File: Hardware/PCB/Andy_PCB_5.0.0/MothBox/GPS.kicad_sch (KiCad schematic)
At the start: 46 parts, among them J4 GPS Header, SW2 Days, SW3 Power, SW4 Sequence+Toggle, SW5 Hours, SW6 Hours, U12 CD74HC4067M96E4, U13 CD74HC4067M96E4

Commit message: made better camera
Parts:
- renumbered C18 to C16, C13 to C17, R28 to R16, R16 to R17, R29 to R18, R17 to R19, R30 to R20, R83 to R21, R18 to R22, R84 to R23, R31 to R24, R85 to R25, R86 to R26, R32 to R27, R19 to R28, R33 to R29, R34 to R30, R20 to R31, R35 to R32, R21 to R33, R36 to R34, R22 to R35, R37 to R36, R23 to R37, R47 to R39, R24 to R40, R39 to R41, R48 to R42, R49 to R43, R50 to R44, R40 to R45, R25 to R46, R41 to R47, R26 to R48, R42 to R49, R27 to R50, U12 to U8, U13 to U9

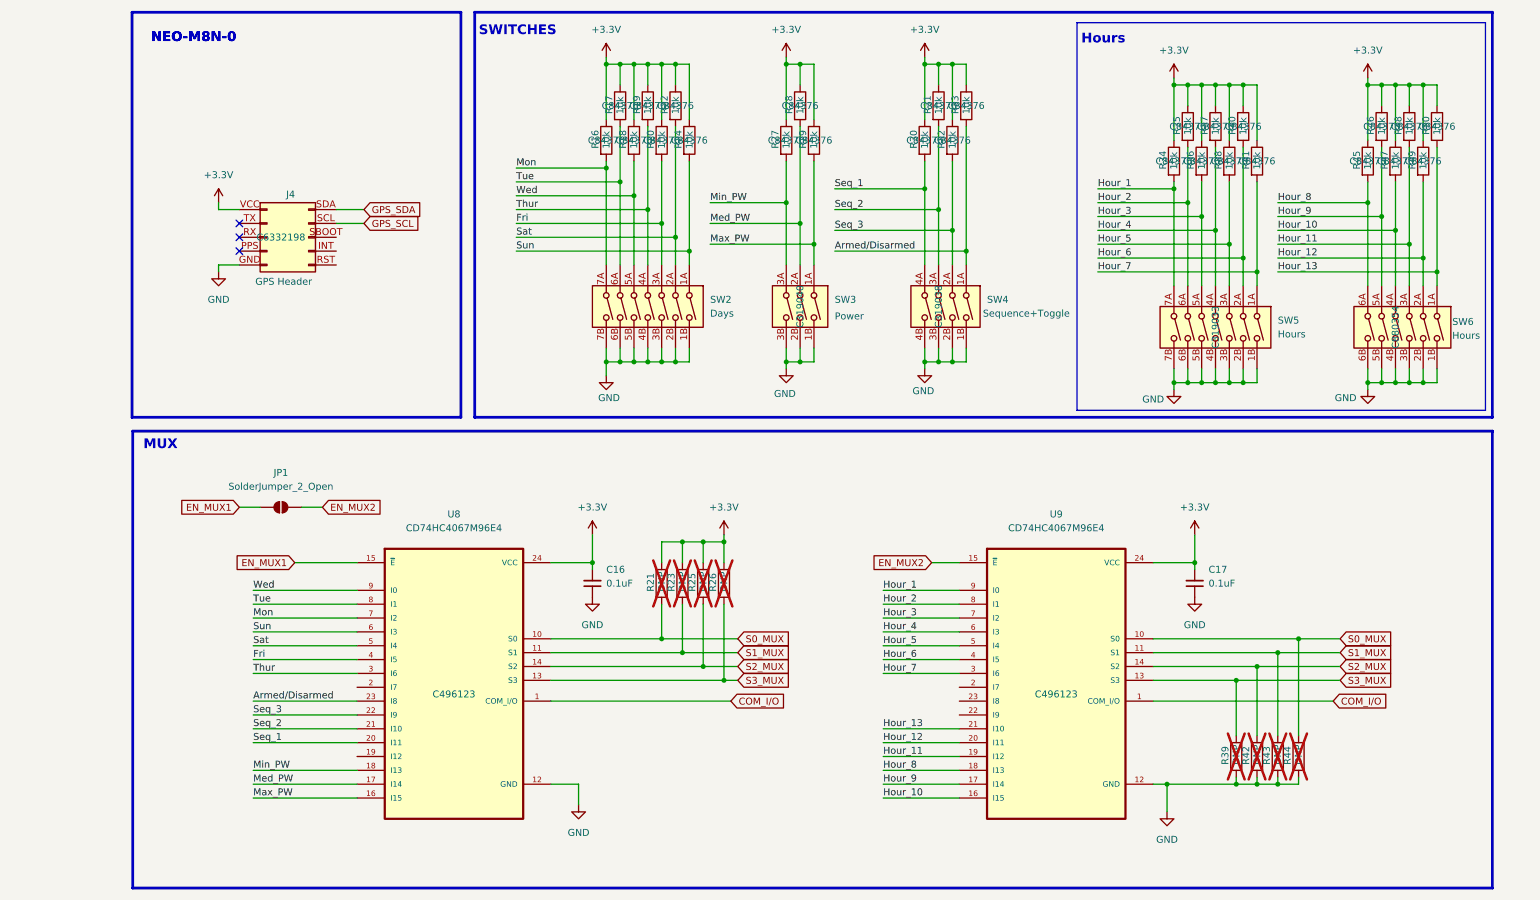
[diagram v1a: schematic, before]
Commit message: added female inverted header
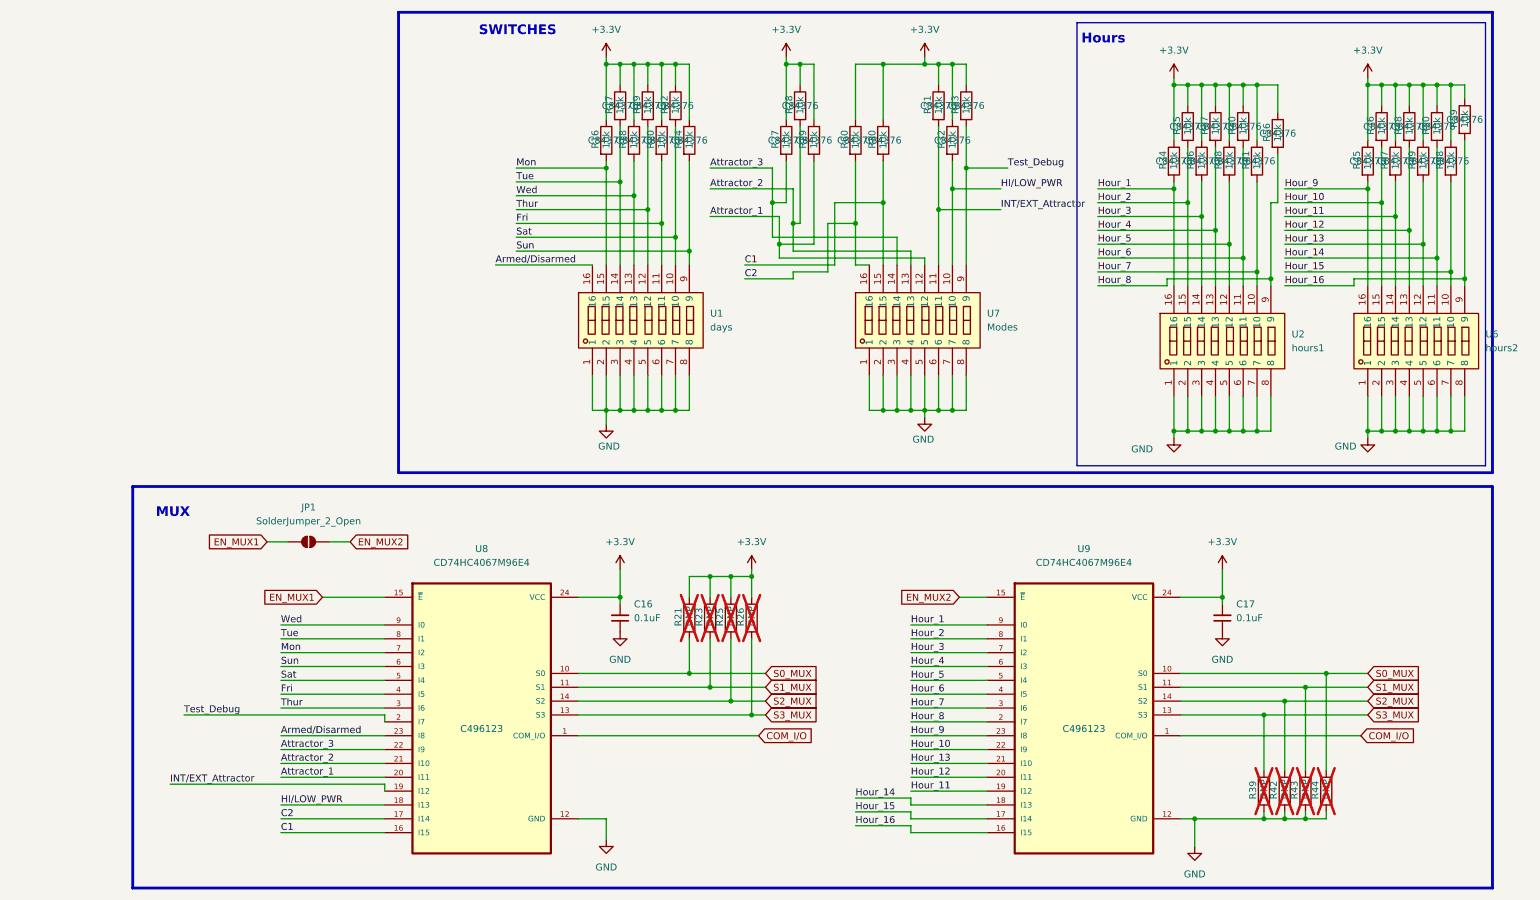
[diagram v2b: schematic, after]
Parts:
- removed J4: GPS Header, GPS_MAX10:Untitled, symbol Connector:DIN41612_02x05_AC_EvenPins
- removed SW2: Days, DS04-254-2-07BK-SMT:SW_DS04-254-2-07BK-SMT, symbol Switch:SW_DIP_x07
- removed SW3: Power, DS04-254-2-03BK-SMT1:SW_DS04-254-2-03BK-SMT, symbol Switch:SW_DIP_x03
- removed SW4: Sequence+Toggle, DS04-254-2-04BK-SMT:SW_DS04-254-2-04BK-SMT, symbol Switch:SW_DIP_x04
- removed SW5: Hours, DS04-254-2-07BK-SMT:SW_DS04-254-2-07BK-SMT, symbol Switch:SW_DIP_x07
- removed SW6: Hours, DS04-254-2-06BK-SMT:SW_DS04-254-2-06BK-SMT, symbol Switch:SW_DIP_x06
- added R56, R58, R59, R60: 10k, Resistor_SMD:R_0805_2012Metric, symbol Device:R
- added U1: days, easyeda2kicad:SW-TH_16P-L21.7-W9.7-P2.54-BL, symbol easyeda2kicad:SMQS-08R-TP
- added U2: hours1, easyeda2kicad:SW-TH_16P-L21.7-W9.7-P2.54-BL, symbol easyeda2kicad:SMQS-08R-TP
- added U6: hours2, easyeda2kicad:SW-TH_16P-L21.7-W9.7-P2.54-BL, symbol easyeda2kicad:SMQS-08R-TP
- added U7: Modes, easyeda2kicad:SW-TH_16P-L21.7-W9.7-P2.54-BL, symbol easyeda2kicad:SMQS-08R-TP
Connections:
- net +3.3V: now also R56.1, R58.1, R59.1, R60.1
- net Armed/Disarmed: now also U1.16; no longer R33.2
- net Fri: now also U1.11
- net GND: now also U1.1, U1.2, U1.3, U1.4, U1.5, U1.6, U1.7, U1.8, U2.1, U2.2, U2.3, U2.4, U2.5, U2.6, U2.7, U2.8, U6.1, U6.2, U6.3, U6.4, U6.5, U6.6, U6.7, U6.8, U7.1, U7.2, U7.3, U7.4, U7.5, U7.6, U7.7, U7.8
- net Hour_1: now also U2.16
- net Hour_10: now also R46.2, U9.22 (I9), U6.15; no longer R47.2, U9.16 (I15)
- net Hour_11: now also R47.2, U6.14; no longer R48.2
- net Hour_12: now also R48.2, U6.13; no longer R49.2
- net Hour_13: now also R49.2, U6.12; no longer R50.2
- net Hour_2: now also U2.15
- net Hour_3: now also U2.14
- net Hour_4: now also U2.13
- net Hour_5: now also U2.12
- net Hour_6: now also U2.11
- net Hour_7: now also U2.10
- net Hour_8: now also U9.2 (I7), R56.2, U2.9; no longer R45.2, U9.18 (I13)
- net Hour_9: now also R45.2, U9.23 (I8), U6.16; no longer R46.2, U9.17 (I14)
- net Mon: now also U1.15
- net Sat: now also U1.10
- net Sun: now also U1.9
- net Thur: now also U1.12
- net Tue: now also U1.14
- net Wed: now also U1.13
- net INT/EXT_Attractor: now reaches U8.19 (I12)
- net INT/EXT_Attractor: now also R31.2, U7.11
- net Test_Debug: now reaches U8.2 (I7)
- net Test_Debug: now also R33.2, U7.9
- net Max_PW renamed Attractor_1
- net Attractor_1: now also U8.20 (I11), U7.12; no longer U8.16 (I15)
- net Med_PW renamed Attractor_2
- net Attractor_2: now also U8.21 (I10), U7.13; no longer U8.17 (I14)
- net Min_PW renamed Attractor_3
- net Attractor_3: now also U8.22 (I9), U7.14; no longer U8.18 (I13)
- net Seq_1 renamed C1
- net C1: now also U8.16 (I15), U7.15; no longer U8.20 (I11)
- removed net Seq_2: R31.2, U8.21 (I10)
- net Seq_3 renamed HI/LOW_PWR
- net HI/LOW_PWR: now also U8.18 (I13), U7.10; no longer U8.22 (I9)
- new net C2: R60.2, U7.16, U8.17 (I14)
- new net Hour_14: R50.2, U6.11, U9.18 (I13)
- new net Hour_15: R58.2, U6.10, U9.17 (I14)
- new net Hour_16: R59.2, U6.9, U9.16 (I15)
- no-connect marks 3 -> 0
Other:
- note removed: "NEO-M8N-0"
- moved on the sheet: C16, C17, JP1, R21, R23, R25, R26, R30, R39, R42, R43, R44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

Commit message: arranged stuff better
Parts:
- U1: value days -> Days
- U2: value hours1 -> Hours1
- U6: value hours2 -> Hours2
- U8, U9: footprint CD74HC4067M96E4:SOIC127P1030X265-24N -> easyeda2kicad:SOIC-24_L15.4-W7.5-P1.27-LS10.3-BL
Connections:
- net EN_MUX1: no longer U8.15 (~{E})
- net EN_MUX2: no longer U9.15 (~{E})
- net GND: now also U8.15 (~{E}), U9.15 (~{E})
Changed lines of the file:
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@@
 	(global_label "EN_MUX1"
 		(shape input)
-		(at 71.12 129.54 180)
-		(fields_autoplaced yes)
-		(effects
-			(font
-				(size 1.27 1.27)
-			)
-			(justify right)
-		)
-		(property "Intersheetrefs" "${INTERSHEET_REFS}"
-			(at 59.4868 129.54 0)
-			(effects
-				(font
-					(size 1.27 1.27)
-				)
-				(justify right)
-				(hide yes)
-			)
-		)
-	)
-	(global_label "EN_MUX1"
-		(shape input)
 		(at 60.96 119.38 180)
 		(fields_autoplaced yes)
@@
 		)
 	)
-	(global_label "EN_MUX2"
-		(shape input)
-		(at 187.96 129.54 180)
-		(fields_autoplaced yes)
-		(effects
-			(font
-				(size 1.27 1.27)
-			)
-			(justify right)
-		)
-		(property "Intersheetrefs" "${INTERSHEET_REFS}"
-			(at 176.3268 129.54 0)
-			(effects
-				(font
-					(size 1.27 1.27)
-				)
-				(justify right)
-				(hide yes)
-			)
-		)
-	)
 	(global_label "S3_MUX"
 		(shape input)
@@
 			)
 		)
-		(property "Footprint" "CD74HC4067M96E4:SOIC127P1030X265-24N"
+		(property "Footprint" "easyeda2kicad:SOIC-24_L15.4-W7.5-P1.27-LS10.3-BL"
 			(at 100.33 137.16 0)
 			(effects
@@
 			)
 		)
-		(property "Value" "hours2"
+		(property "Value" "Hours2"
 			(at 284.48 83.8199 0)
 			(effects
@@
 			)
 		)
-		(property "Value" "hours1"
+		(property "Value" "Hours1"
 			(at 248.92 83.8199 0)
 			(effects
@@
 			)
 		)
-		(property "Value" "days"
+		(property "Value" "Days"
 			(at 142.24 80.0099 0)
 			(effects
@@
 			)
 		)
-		(property "Footprint" "CD74HC4067M96E4:SOIC127P1030X265-24N"
+		(property "Footprint" "easyeda2kicad:SOIC-24_L15.4-W7.5-P1.27-LS10.3-BL"
 			(at 210.82 137.16 0)
 			(effects
@@
 	)
 	(symbol
+		(lib_id "power:GND")
+		(at 71.12 129.54 270)
+		(unit 1)
+		(exclude_from_sim no)
+		(in_bom yes)
+		(on_board yes)
+		(dnp no)
+		(fields_autoplaced yes)
+		(property "Reference" "#PWR05"
+			(at 64.77 129.54 0)
+			(effects
+				(font
+					(size 1.27 1.27)
+				)
+				(hide yes)
+			)
+		)
+		(property "Value" "GND"
+			(at 67.31 129.5399 90)
+			(effects
+				(font
+					(size 1.27 1.27)
+				)
+				(justify right)
+			)
+		)
+		(property "Footprint" ""
+			(at 71.12 129.54 0)
+			(effects
+				(font
+					(size 1.27 1.27)
+				)
+				(hide yes)
+			)
+		)
+		(property "Datasheet" ""
+			(at 71.12 129.54 0)
+			(effects
+				(font
+					(size 1.27 1.27)
+				)
+				(hide yes)
+			)
+		)
+		(property "Description" "Power symbol creates a global label with name \"GND\" , ground"
+			(at 71.12 129.54 0)
+			(effects
+				(font
+					(size 1.27 1.27)
+				)
+				(hide yes)
+			)
+		)
+		(pin "1"
+		)
+		(instances
+			(project "MothBox"
+				(path "/9021e528-fc76-4423-a3f3-30f5652071cc/d22974ea-9095-4b9a-829f-a5d553626ed9"
+					(reference "#PWR05")
+					(unit 1)
+				)
+			)
+		)
+	)
+	(symbol
 		(lib_id "Device:R")
 		(at 156.21 45.72 0)
@@
 					(unit 1)
 				)
+			)
+		)
+	)
+	(symbol
+		(lib_id "power:GND")
+		(at 187.96 129.54 270)
+		(unit 1)
+		(exclude_from_sim no)
+		(in_bom yes)
+		(on_board yes)
+		(dnp no)
+		(fields_autoplaced yes)
+		(property "Reference" "#PWR08"
+			(at 181.61 129.54 0)
+			(effects
+				(font
+					(size 1.27 1.27)
+				)
+				(hide yes)
+			)
+		)
+		(property "Value" "GND"
+			(at 184.15 129.5399 90)
+			(effects
+				(font
+					(size 1.27 1.27)
+				)
+				(justify right)
+			)
+		)
+		(property "Footprint" ""
+			(at 187.96 129.54 0)
+			(effects
+				(font
+					(size 1.27 1.27)
+				)
+				(hide yes)
+			)
+		)
+		(property "Datasheet" ""
+			(at 187.96 129.54 0)
+			(effects
+				(font
+					(size 1.27 1.27)
+				)
+				(hide yes)
+			)
+		)
+		(property "Description" "Power symbol creates a global label with name \"GND\" , ground"
+			(at 187.96 129.54 0)
+			(effects
+				(font
+					(size 1.27 1.27)
+				)
+				(hide yes)
+			)
+		)
+		(pin "1"
+		)
+		(instances
+			(project "MothBox"
+				(path "/9021e528-fc76-4423-a3f3-30f5652071cc/d22974ea-9095-4b9a-829f-a5d553626ed9"
+					(reference "#PWR08")
+					(unit 1)
+				)

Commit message: made regulator switch on and off and SMD switches
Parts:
- U1, U2, U6, U7: footprint easyeda2kicad:SW-TH_16P-L21.7-W9.7-P2.54-BL -> easyeda2kicad:SW-SMD_SMXS-08K-TP; symbol easyeda2kicad:SMQS-08R-TP -> easyeda2kicad:SMXS-08K-TP; LCSC Part C5299509 -> C5439767
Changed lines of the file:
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@@
 	)
 	(symbol
-		(lib_id "easyeda2kicad:SMQS-08R-TP")
+		(lib_id "easyeda2kicad:SMXS-08K-TP")
 		(at 273.05 82.55 0)
 		(unit 1)
@@
 			)
 		)
-		(property "Footprint" "easyeda2kicad:SW-TH_16P-L21.7-W9.7-P2.54-BL"
+		(property "Footprint" "easyeda2kicad:SW-SMD_SMXS-08K-TP"
 			(at 273.05 100.33 0)
 			(effects
@@
 			)
 		)
-		(property "LCSC Part" "C5299509"
+		(property "LCSC Part" "C5439767"
 			(at 273.05 102.87 0)
 			(effects
@@
 	)
 	(symbol
-		(lib_id "easyeda2kicad:SMQS-08R-TP")
+		(lib_id "easyeda2kicad:SMXS-08K-TP")
 		(at 181.61 78.74 0)
 		(unit 1)
@@
 			)
 		)
-		(property "Footprint" "easyeda2kicad:SW-TH_16P-L21.7-W9.7-P2.54-BL"
+		(property "Footprint" "easyeda2kicad:SW-SMD_SMXS-08K-TP"
 			(at 181.61 96.52 0)
 			(effects
@@
 			)
 		)
-		(property "LCSC Part" "C5299509"
+		(property "LCSC Part" "C5439767"
 			(at 181.61 99.06 0)
 			(effects
@@
 	)
 	(symbol
-		(lib_id "easyeda2kicad:SMQS-08R-TP")
+		(lib_id "easyeda2kicad:SMXS-08K-TP")
 		(at 237.49 82.55 0)
 		(unit 1)
@@
 			)
 		)
-		(property "Footprint" "easyeda2kicad:SW-TH_16P-L21.7-W9.7-P2.54-BL"
+		(property "Footprint" "easyeda2kicad:SW-SMD_SMXS-08K-TP"
 			(at 237.49 100.33 0)
 			(effects
@@
 			)
 		)
-		(property "LCSC Part" "C5299509"
+		(property "LCSC Part" "C5439767"
 			(at 237.49 102.87 0)
 			(effects
@@
 	)
 	(symbol
-		(lib_id "easyeda2kicad:SMQS-08R-TP")
+		(lib_id "easyeda2kicad:SMXS-08K-TP")
 		(at 130.81 78.74 0)
 		(unit 1)
@@
 			)
 		)
-		(property "Footprint" "easyeda2kicad:SW-TH_16P-L21.7-W9.7-P2.54-BL"
+		(property "Footprint" "easyeda2kicad:SW-SMD_SMXS-08K-TP"
 			(at 130.81 96.52 0)
 			(effects
@@
 			)
 		)
-		(property "LCSC Part" "C5299509"
+		(property "LCSC Part" "C5439767"
 			(at 130.81 99.06 0)
 			(effects

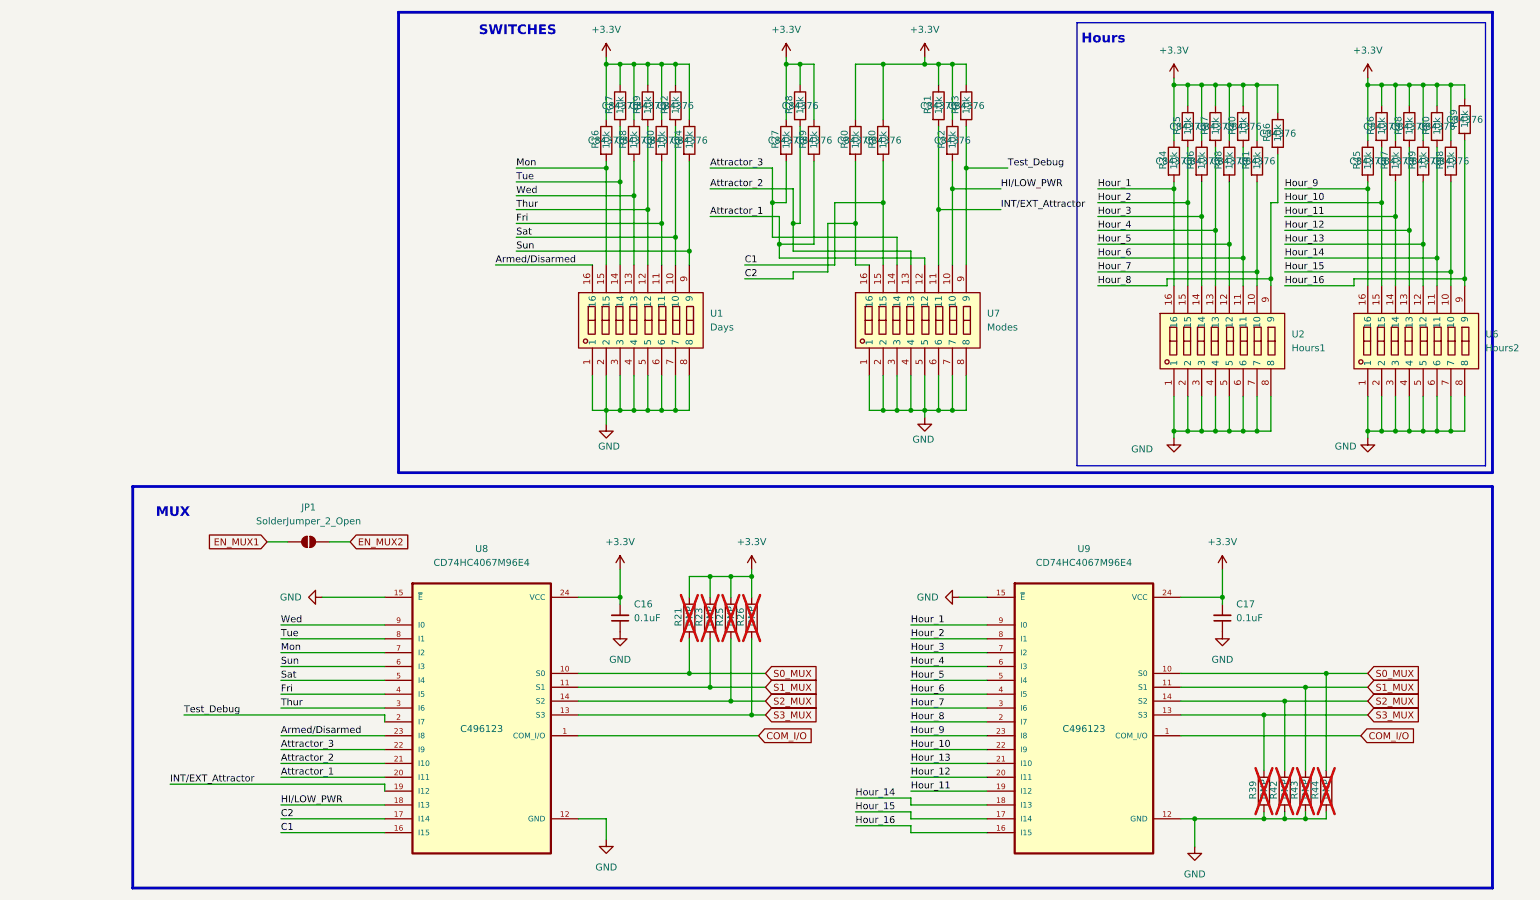
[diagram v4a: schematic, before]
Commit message: added GPS 2 kinds
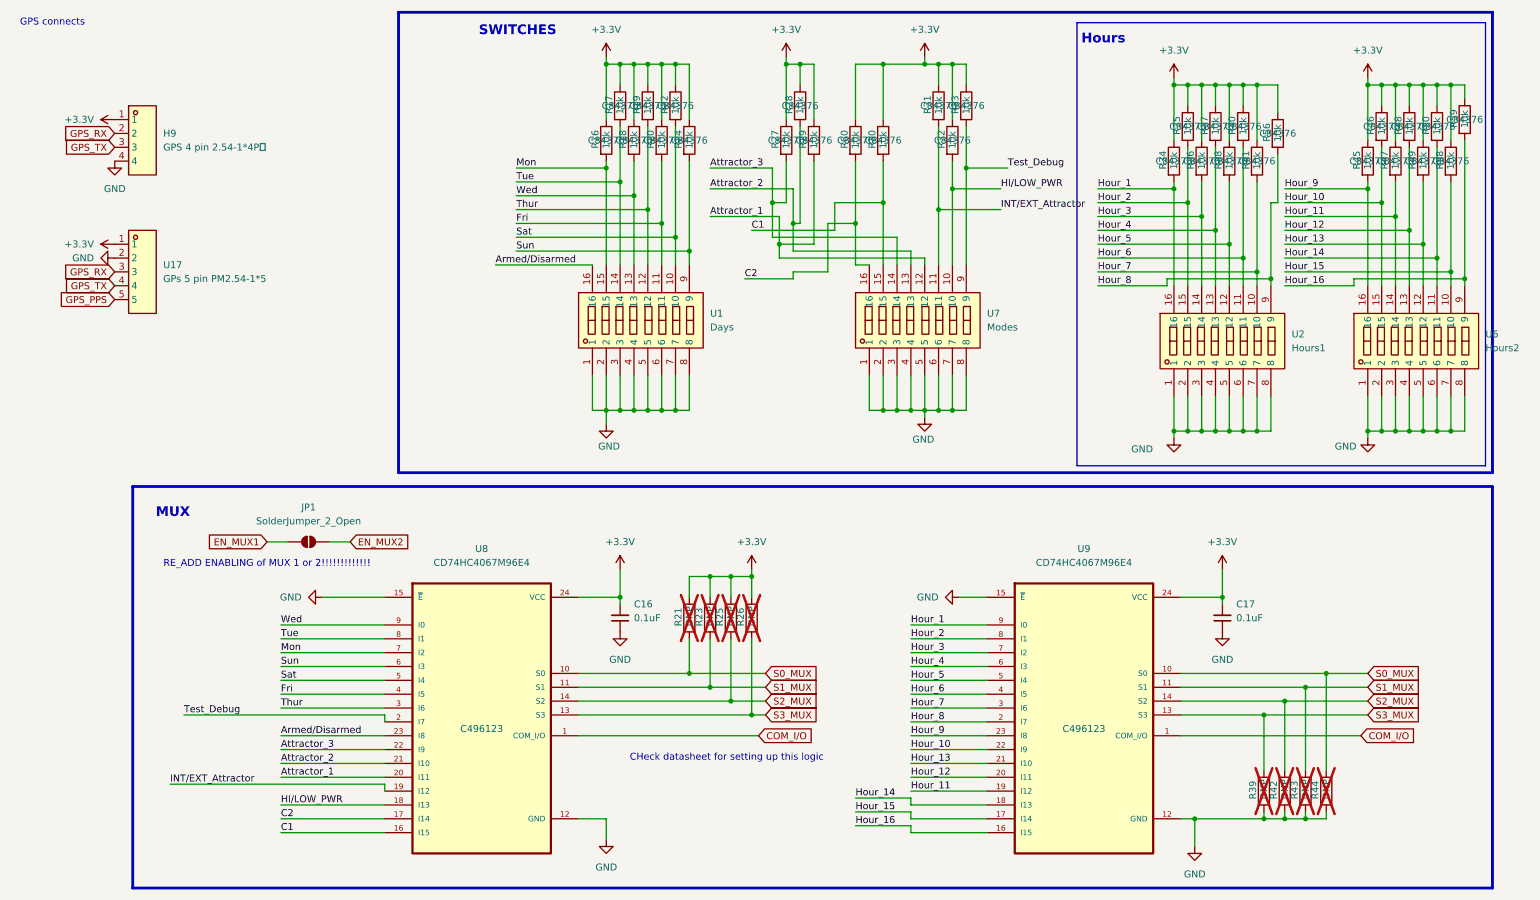
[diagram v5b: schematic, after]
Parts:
- added H9: GPS 4 pin 2.54-1*4P母, AQLibrary:GPS4pin_HDR-TH_4P-P2.54-V-F, symbol easyeda2kicad:2.54-1*4P母
- added U17: GPs 5 pin PM2.54-1*5, AQLibrary:GPS5pin_HDR-TH_5P-P2.54-V-F, symbol easyeda2kicad:PM2.54-1*5
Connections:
- net +3.3V: now also H9.1, U17.1
- net GND: now also H9.4, U17.2
- new net GPS_PPS: U17.5
- new net GPS_RX: H9.2, U17.3
- new net GPS_TX: H9.3, U17.4
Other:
- note added: "CHeck datasheet for setting up this logic"
- note added: "GPS connects"
- note added: "RE_ADD ENABLING of MUX 1 or 2!!!!!!!!!!!!!"
